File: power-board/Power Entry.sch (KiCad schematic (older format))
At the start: 13 parts, among them J1 CONN_01X02, Q1 Q_NMOS_DGS, U4 RT1720

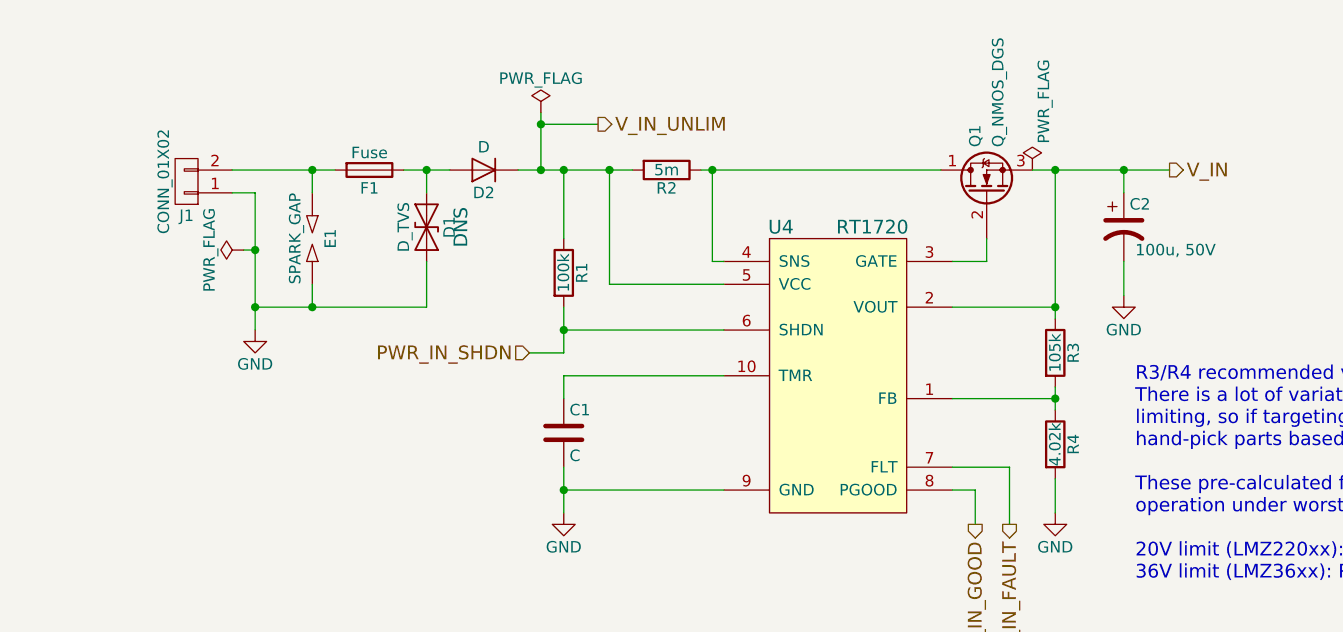
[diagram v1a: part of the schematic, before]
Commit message: switched to XMEGA A4U
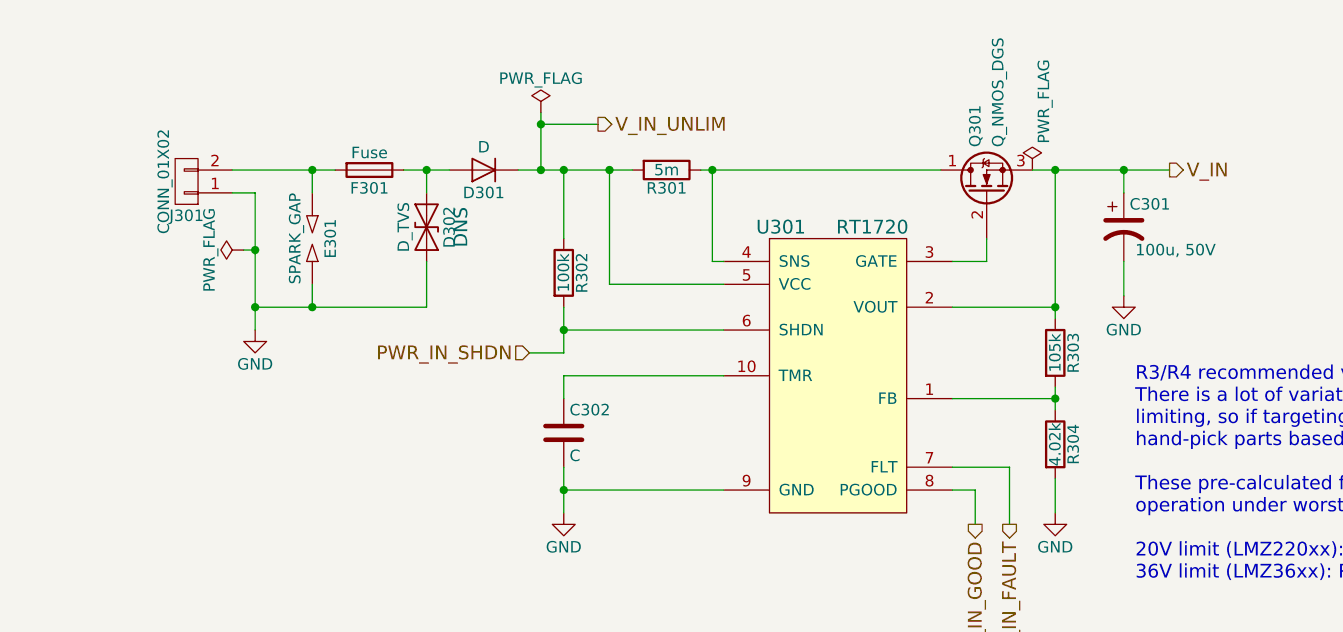
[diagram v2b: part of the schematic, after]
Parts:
- renumbered C2 to C301, C1 to C302, D2 to D301, D1 to D302, E1 to E301, F1 to F301, J1 to J301, Q1 to Q301, R2 to R301, R1 to R302, R3 to R303, R4 to R304, U4 to U301
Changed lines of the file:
@@
 $Descr A4 11693 8268
 encoding utf-8
-Sheet 3 10
+Sheet 3 11
 Title ""
 Date ""
@@
 $EndDescr
 $Comp
-L CONN_01X02 J1
+L CONN_01X02 J301
 U 1 1 5934B3F8
 P 2950 3050
-F 0 "J1" H 2950 3200 50  0000 C CNN
+F 0 "J301" H 2950 3200 50  0000 C CNN
 F 1 "CONN_01X02" V 3050 3050 50  0000 C CNN
 F 2 "" H 2950 3050 50  0001 C CNN
@@
 $EndComp
 $Comp
-L D_TVS D1
+L D_TVS D302
 U 1 1 5934B400
 P 4000 3250
-F 0 "D1" H 4000 3350 50  0000 C CNN
+F 0 "D302" H 4000 3350 50  0000 C CNN
 F 1 "D_TVS" H 4000 3150 50  0000 C CNN
 F 2 "" H 4000 3250 50  0001 C CNN
@@
 $EndComp
 $Comp
-L CP1 C2
+L CP1 C301
 U 1 1 5934B408
 P 7050 3250
-F 0 "C2" H 7075 3350 50  0000 L CNN
+F 0 "C301" H 7075 3350 50  0000 L CNN
 F 1 "100u, 50V" H 7100 3150 50  0000 L CNN
 F 2 "" H 7050 3250 50  0001 C CNN
@@
 $EndComp
 $Comp
-L Fuse F1
+L Fuse F301
 U 1 1 5934B417
 P 3750 3000
-F 0 "F1" V 3830 3000 50  0000 C CNN
+F 0 "F301" V 3830 3000 50  0000 C CNN
 F 1 "Fuse" V 3675 3000 50  0000 C CNN
 F 2 "" V 3680 3000 50  0001 C CNN
@@
 $EndComp
 $Comp
-L D D2
+L D D301
 U 1 1 5934B41E
 P 4250 3000
-F 0 "D2" H 4250 3100 50  0000 C CNN
+F 0 "D301" H 4250 3100 50  0000 C CNN
 F 1 "D" H 4250 2900 50  0000 C CNN
 F 2 "" H 4250 3000 50  0001 C CNN
@@
 $EndComp
 $Comp
-L SPARK_GAP E1
+L SPARK_GAP E301
 U 1 1 5934B425
 P 3500 3300
-F 0 "E1" H 3500 3380 50  0000 C CNN
+F 0 "E301" H 3500 3380 50  0000 C CNN
 F 1 "SPARK_GAP" H 3500 3225 50  0000 C CNN
 F 2 "" H 3500 3230 50  0001 C CNN
@@
 $EndComp
 $Comp
-L RT1720 U4
+L RT1720 U301
 U 1 1 5934B434
 P 5500 3300
-F 0 "U4" H 5550 3350 60  0000 C CNN
+F 0 "U301" H 5550 3350 60  0000 C CNN
 F 1 "RT1720" H 5950 3350 60  0000 C CNN
 F 2 "" H 5500 3300 60  0001 C CNN
@@
 $EndComp
 $Comp
-L R R1
+L R R302
 U 1 1 5934B43B
 P 4600 3450
-F 0 "R1" V 4680 3450 50  0000 C CNN
+F 0 "R302" V 4680 3450 50  0000 C CNN
 F 1 "100k" V 4600 3450 50  0000 C CNN
 F 2 "" V 4530 3450 50  0001 C CNN
@@
 $EndComp
 $Comp
-L C C1
+L C C302
 U 1 1 5934B442
 P 4600 4150
-F 0 "C1" H 4625 4250 50  0000 L CNN
+F 0 "C302" H 4625 4250 50  0000 L CNN
 F 1 "C" H 4625 4050 50  0000 L CNN
 F 2 "" H 4638 4000 50  0001 C CNN
@@
 $EndComp
 $Comp
-L GND #PWR17
+L GND #PWR015
 U 1 1 5934B449
 P 4600 4500
-F 0 "#PWR17" H 4600 4250 50  0001 C CNN
+F 0 "#PWR015" H 4600 4250 50  0001 C CNN
 F 1 "GND" H 4600 4350 50  0000 C CNN
 F 2 "" H 4600 4500 50  0001 C CNN
@@
 $EndComp
 $Comp
-L Q_NMOS_DGS Q1
+L Q_NMOS_DGS Q301
 U 1 1 5934B44F
 P 6450 3100
-F 0 "Q1" H 6650 3150 50  0000 L CNN
+F 0 "Q301" H 6650 3150 50  0000 L CNN
 F 1 "Q_NMOS_DGS" H 6650 3050 50  0000 L CNN
 F 2 "" H 6650 3200 50  0001 C CNN
@@
 $EndComp
 $Comp
-L R R2
+L R R301
 U 1 1 5934B456
 P 5050 3000
-F 0 "R2" V 5130 3000 50  0000 C CNN
+F 0 "R301" V 5130 3000 50  0000 C CNN
 F 1 "5m" V 5050 3000 50  0000 C CNN
 F 2 "" V 4980 3000 50  0001 C CNN
@@
 $EndComp
 $Comp
-L R R3
+L R R303
 U 1 1 5934B45D
 P 6750 3800
-F 0 "R3" V 6830 3800 50  0000 C CNN
+F 0 "R303" V 6830 3800 50  0000 C CNN
 F 1 "105k" V 6750 3800 50  0000 C CNN
 F 2 "" V 6680 3800 50  0001 C CNN
@@
 $EndComp
 $Comp
-L R R4
+L R R304
 U 1 1 5934B464
 P 6750 4200
-F 0 "R4" V 6830 4200 50  0000 C CNN
+F 0 "R304" V 6830 4200 50  0000 C CNN
 F 1 "4.02k" V 6750 4200 50  0000 C CNN
 F 2 "" V 6680 4200 50  0001 C CNN
@@
 $EndComp
 $Comp
-L GND #PWR18
+L GND #PWR016
 U 1 1 5934B46B
 P 6750 4500
-F 0 "#PWR18" H 6750 4250 50  0001 C CNN
+F 0 "#PWR016" H 6750 4250 50  0001 C CNN
 F 1 "GND" H 6750 4350 50  0000 C CNN
 F 2 "" H 6750 4500 50  0001 C CNN
@@
 $EndComp
 $Comp
-L GND #PWR15
+L GND #PWR017
 U 1 1 5934B473
 P 7050 3550
-F 0 "#PWR15" H 7050 3300 50  0001 C CNN
+F 0 "#PWR017" H 7050 3300 50  0001 C CNN
 F 1 "GND" H 7050 3400 50  0000 C CNN
 F 2 "" H 7050 3550 50  0001 C CNN
@@
 	5300 3500 4800 3500
 $Comp
-L GND #PWR16
+L GND #PWR018
 U 1 1 5934B4B9
 P 3250 3700
-F 0 "#PWR16" H 3250 3450 50  0001 C CNN
+F 0 "#PWR018" H 3250 3450 50  0001 C CNN
 F 1 "GND" H 3250 3550 50  0000 C CNN
 F 2 "" H 3250 3700 50  0001 C CNN
@@
 R3/R4 recommended values (based on 1% resistors):\nThere is a lot of variation in the specified performance of the voltage\nlimiting, so if targeting a highly accurate limit, you will likely have to\nhand-pick parts based on the FB performance of the particular unit.\n\nThese pre-calculated figures err on the low side, to ensure safe\noperation under worst-case device parameters.\n\n20V limit (LMZ220xx): R3 = 97.6k, R4 = 6.81k\n36V limit (LMZ36xx): R3 = 105k, R4 = 4.02k
 $Comp
-L PWR_FLAG #FLG2
+L PWR_FLAG #FLG019
 U 1 1 593A6C03
 P 6650 3000
-F 0 "#FLG2" H 6650 3075 50  0001 C CNN
+F 0 "#FLG019" H 6650 3075 50  0001 C CNN
 F 1 "PWR_FLAG" V 6700 3300 50  0000 C CNN
 F 2 "" H 6650 3000 50  0001 C CNN
@@
 $EndComp
 $Comp
-L PWR_FLAG #FLG3
+L PWR_FLAG #FLG020
 U 1 1 593A7194
 P 3200 3350
-F 0 "#FLG3" H 3200 3425 50  0001 C CNN
+F 0 "#FLG020" H 3200 3425 50  0001 C CNN
 F 1 "PWR_FLAG" H 3200 3500 50  0000 C CNN
 F 2 "" H 3200 3350 50  0001 C CNN
@@
 Connection ~ 3500 3600
 $Comp
-L PWR_FLAG #FLG1
+L PWR_FLAG #FLG021
 U 1 1 593A7954
 P 4500 2750
-F 0 "#FLG1" H 4500 2825 50  0001 C CNN
+F 0 "#FLG021" H 4500 2825 50  0001 C CNN
 F 1 "PWR_FLAG" H 4500 2900 50  0000 C CNN
 F 2 "" H 4500 2750 50  0001 C CNN

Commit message: routed board
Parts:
- removed D301: D, symbol D
- removed Q301: Q_NMOS_DGS, symbol Q_NMOS_DGS
- added D301: 5A, Diodes_SMD:D_SMC_Standard, symbol D_Schottky
- added Q301: Q_NMOS_SSSGD, TO_SOT_Packages_SMD:SOT-669_LFPAK_ThermalVias-1, symbol Q_NMOS_SSSGD
- C301: value 100u, 50V -> 330u, 50V; footprint (none) -> Capacitors_THT:CP_Radial_D10.0mm_P5.00mm; MFG Wurth Electronics Inc. -> Panasonic Electronic Components; MPN 865080653016 -> ECA-1HM331
- C302: footprint (none) -> Capacitors_SMD:C_0805
- D302: value D_TVS -> 36V; footprint (none) -> Diodes_SMD:D_SMA_Standard; MFG (none) -> Wurth Electronics Inc.; MPN (none) -> 824501361; Note DNS -> (none)
- E301: footprint (none) -> project:Spark_Gap_8mil
- F301: value Fuse -> 4.5A; footprint (none) -> Resistors_SMD:R_0603_HandSoldering; MFG (none) -> Littelfuse; MPN (none) -> 0603SFS450F/32-2; Note (none) -> OPT
- J301: footprint (none) -> Connectors_Terminal_Blocks:TerminalBlock_Pheonix_PT-3.5mm_2pol
- R301: value 5m -> 10m; footprint (none) -> Resistors_SMD:R_1206; MFG (none) -> Samsung; MPN (none) -> RU3216FR010CS
- R302: footprint (none) -> Resistors_SMD:R_0603; MFG Vishay / Draloric -> Yageo; MPN RCA0603100KJNEC -> RC0603JR-07100KL
- R303: footprint (none) -> Resistors_SMD:R_0805; MFG Bourns -> Yageo; MPN CR0603-FX-1053ELF -> RC0805FR-07105KL
- R304: footprint (none) -> Resistors_SMD:R_0805; MFG (none) -> Yageo; MPN (none) -> RC0805FR-074K02L
- U301: footprint (none) -> Housings_SSOP:MSOP-10_3x3mm_Pitch0.5mm
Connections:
- net V_IN: now also Q301.1 (S), Q301.2 (S), Q301.3 (S)
- net V_IN_UNLIM: now also D301.1 (K)
- net V_IN_UNFUSED: now reaches E301.1, F301.2, J301.2 (P2)
- net V_IN_FUSED: now reaches D302.1 (A1), F301.1
- net V_IN_FUSED: now also D301.2 (A)
- net V_IN_LIM_FB: now reaches R303.2, R304.1, U301.1 (FB)
- net V_IN_TMR: now reaches C302.1, U301.10 (TMR)
- net V_IN_GATE_DRV: now reaches U301.3 (GATE)
- net V_IN_GATE_DRV: now also Q301.4 (G)
- net V_IN_SENSE: now reaches R301.1, U301.4 (SNS)
- net V_IN_SENSE: now also Q301.5 (D)

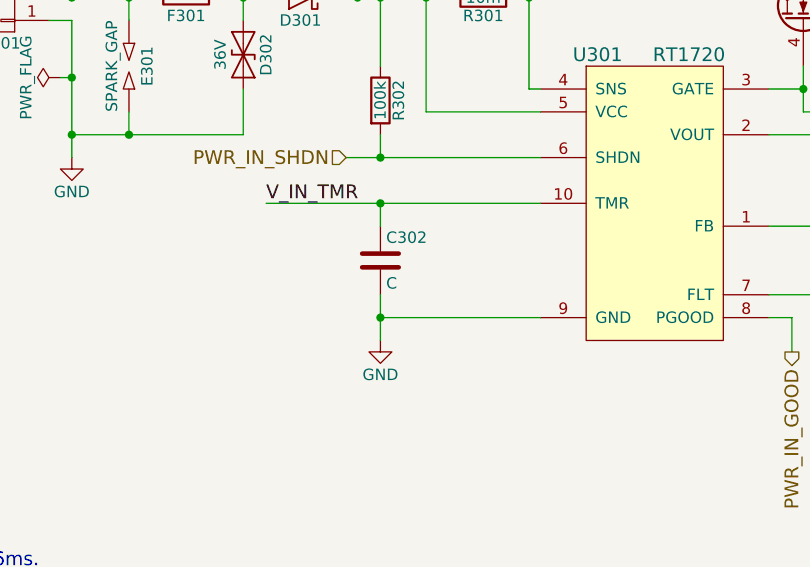
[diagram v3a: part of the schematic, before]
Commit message: adding more part numbers
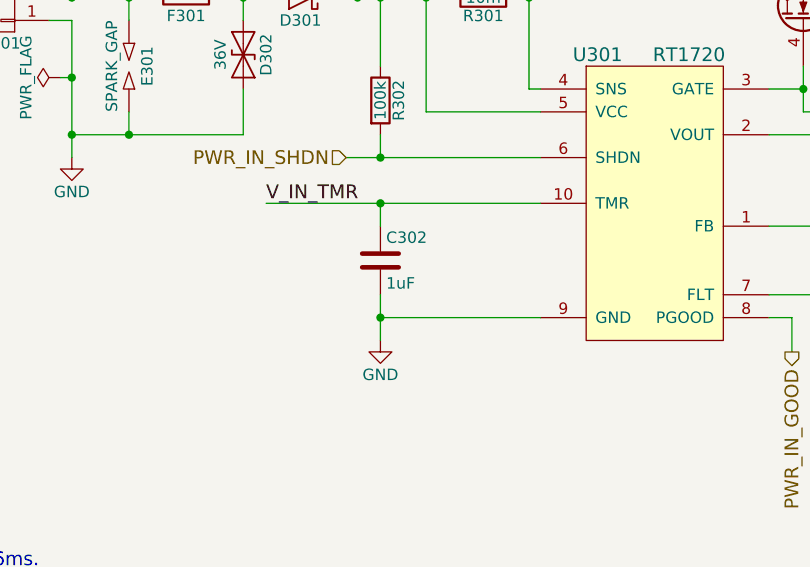
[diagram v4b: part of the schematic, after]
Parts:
- C302: value C -> 1uF; MFG (none) -> Yageo; MPN (none) -> CC0805ZRY5V7BB105
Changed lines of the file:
@@
 P 4600 4150
 F 0 "C302" H 4625 4250 50  0000 L CNN
-F 1 "C" H 4625 4050 50  0000 L CNN
+F 1 "1uF" H 4625 4050 50  0000 L CNN
 F 2 "Capacitors_SMD:C_0805" H 4638 4000 50  0001 C CNN
 F 3 "" H 4600 4150 50  0001 C CNN
+F 4 "Yageo" H 4600 4150 60  0001 C CNN "MFG"
+F 5 "CC0805ZRY5V7BB105" H 4600 4150 60  0001 C CNN "MPN"
 	1    4600 4150
 	1    0    0    -1

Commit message: finished up parts ordering and generated gerbers
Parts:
- J301: MFG (none) -> Phoenix Contact; MPN (none) -> 1984617
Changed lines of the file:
@@
 F 2 "Connectors_Terminal_Blocks:TerminalBlock_Pheonix_PT-3.5mm_2pol" H 2950 3050 50  0001 C CNN
 F 3 "" H 2950 3050 50  0001 C CNN
+F 4 "Phoenix Contact" H 2950 3050 60  0001 C CNN "MFG"
+F 5 "1984617" H 2950 3050 60  0001 C CNN "MPN"
 	1    2950 3050
 	-1   0    0    1
